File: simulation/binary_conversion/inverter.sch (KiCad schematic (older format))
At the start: 4 parts, among them M1 BSS84, M2 2N7002

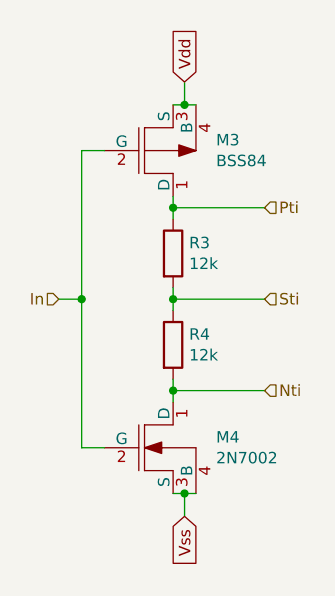
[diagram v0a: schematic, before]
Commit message: ternary adders, switches, and cyclers
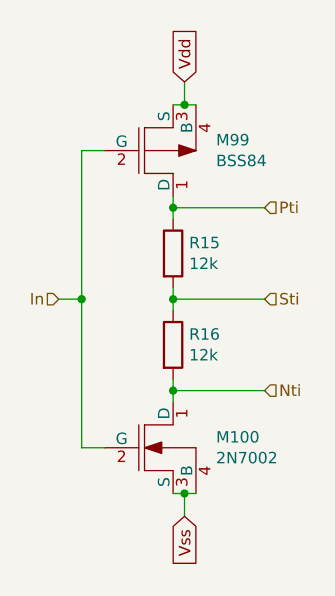
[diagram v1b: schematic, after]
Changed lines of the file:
@@
 $Descr A4 11693 8268
 encoding utf-8
-Sheet 65 64
+Sheet 9 91
 Title ""
 Date ""
@@
 AR Path="/639E88A2/5FCF511D/5FCC772E" Ref="M?"  Part="1"
 AR Path="/639E88A8/5FCF511D/5FCC772E" Ref="M4"  Part="1"
-F 0 "M4" H 5788 4596 50  0000 L CNN
+F 0 "M100" H 5788 4596 50  0000 L CNN
 F 1 "2N7002" H 5788 4505 50  0000 L CNN
 F 2 "" H 5475 4550 50  0001 C CNN
@@
 AR Path="/639E88A2/5FCF511D/5FCC81EB" Ref="M?"  Part="1"
 AR Path="/639E88A8/5FCF511D/5FCC81EB" Ref="M3"  Part="1"
-F 0 "M3" H 5788 3296 50  0000 L CNN
+F 0 "M99" H 5788 3296 50  0000 L CNN
 F 1 "BSS84" H 5788 3205 50  0000 L CNN
 F 2 "" H 5500 3250 50  0001 C CNN
@@
 AR Path="/639E88A2/5FCF511D/5FCCA063" Ref="R?"  Part="1"
 AR Path="/639E88A8/5FCF511D/5FCCA063" Ref="R3"  Part="1"
-F 0 "R3" H 5670 3746 50  0000 L CNN
+F 0 "R15" H 5670 3746 50  0000 L CNN
 F 1 "12k" H 5670 3655 50  0000 L CNN
 F 2 "" V 5530 3700 50  0001 C CNN
@@
 AR Path="/639E88A2/5FCF511D/5FCCB8C8" Ref="R?"  Part="1"
 AR Path="/639E88A8/5FCF511D/5FCCB8C8" Ref="R4"  Part="1"
-F 0 "R4" H 5670 4146 50  0000 L CNN
+F 0 "R16" H 5670 4146 50  0000 L CNN
 F 1 "12k" H 5670 4055 50  0000 L CNN
 F 2 "" V 5530 4100 50  0001 C CNN
